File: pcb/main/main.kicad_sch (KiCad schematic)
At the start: 19 parts

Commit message: chore: add circuit git changes
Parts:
- removed C? (x6): 0.1u, Capacitor_SMD:C_0201_0603Metric, symbol Device:C_Small
- removed C? (x2): 2.2u, Capacitor_SMD:C_0402_1005Metric, symbol Device:C_Small
- removed C?: 1u, Capacitor_SMD:C_0201_0603Metric, symbol Device:C_Small
- removed C? (x2): 15p, symbol Device:C_Small
- removed C?: 4.7u, Capacitor_SMD:C_0402_1005Metric, symbol Device:C_Small
- removed C?: 0.01u, Capacitor_SMD:C_0402_1005Metric, symbol Device:C_Small
- removed R?: 1k, symbol Device:R_Small
- removed R?: 330, symbol Device:R_Small
- removed R?: 10k, symbol Device:R_Small
- removed SW?: TVAF06-A020B-R, half_mouse_lib:TVAF06-A020B-R, symbol My_Device:SKRPACE
- removed U?: STM32F405RGTx, Package_QFP:LQFP-64_10x10mm_P0.5mm, symbol MCU_ST_STM32F4:STM32F405RGTx
- removed Y?: 16MHz, symbol Device:Crystal_GND2_Small
- added C17: 150u, Capacitor_SMD:CP_Elec_8x10.5, symbol Device:C_Polarized_Small_US
- added J1: XT60PW-M, Connector_AMASS:AMASS_XT60-F_1x02_P7.20mm_Vertical, symbol Connector_Generic:Conn_01x02
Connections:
- net GND: now also C17.2, J1.1 (Pin_1)
- new net +BATT: C17.1, J1.2 (Pin_2)
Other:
- removed sheet COM
- removed sheet user_interface
- added sheet stm32f405rg (stm32f405rg.kicad_sch)
- sheet can ports: added CAN_H, CAN_L; removed CAN_RX, CAN_TX, LED1_RX, LED1_TX, LED2_RX, LED2_TX, LED3_RX, LED3_TX
- sheet imu ports: added CS_IMU1, CS_IMU2, CS_IMU3, CS_IMU4, CS_IMU5, CS_IMU6, SPI_CLK, SPI_MISO, SPI_MOSI; removed CLK, CS1, CS2, CS3, CS4, CS5, CS6, MISO, MOSI

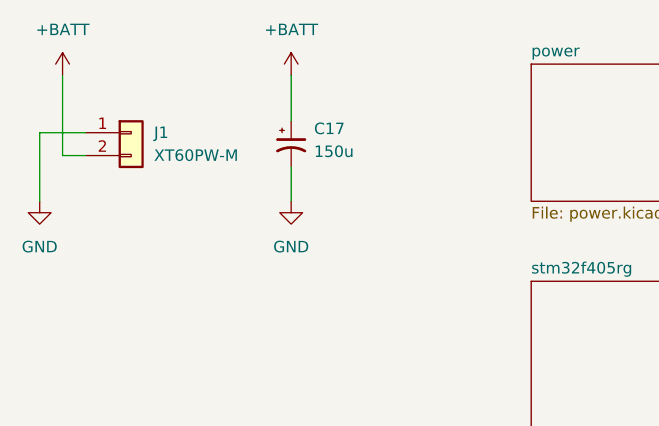
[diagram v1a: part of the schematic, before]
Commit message: perf: update LCD and microSD
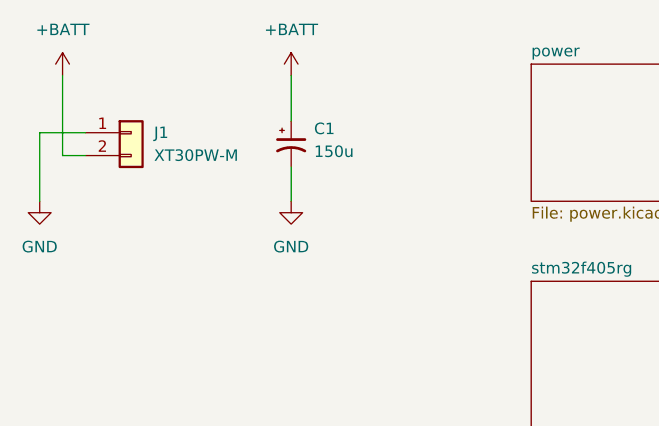
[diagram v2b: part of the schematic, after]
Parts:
- J1: value XT60PW-M -> XT30PW-M; footprint Connector_AMASS:AMASS_XT60-F_1x02_P7.20mm_Vertical -> Connector_AMASS:AMASS_XT30U-F_1x02_P5.0mm_Vertical
- renumbered C17 to C1
